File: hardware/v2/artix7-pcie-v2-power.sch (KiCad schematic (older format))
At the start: 40 parts, among them U3 LP5907MFX-1.2, U5 TPS82130SILT, U6 TPS82150SILT, U7 TPS82150SILT, U8 TPS82130SILT, U9 TPS82150SILT

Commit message: v2 hardware : fix isues found by jlcpcb - change 0603 parts to add paste as they are now loaded - fix solder paste/mask issues with TPS power modules
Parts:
- R40, R41: footprint tom-passives:R_0603_1608Metric_NoPaste -> tom-passives:R_0603_1608Metric
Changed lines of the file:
@@
 F 0 "R40" H 1921 6988 40  0000 L CNN
 F 1 "0R" H 1921 6912 40  0000 L CNN
-F 2 "tom-passives:R_0603_1608Metric_NoPaste" H 1921 6874 30  0001 L CNN
+F 2 "tom-passives:R_0603_1608Metric" H 1921 6874 30  0001 L CNN
 F 3 "" H 1850 6950 30  0001 C CNN
 F 4 "C21189" H 1850 6950 50  0001 C CNN "LCSC"
@@
 F 0 "R41" H 2271 6788 40  0000 L CNN
 F 1 "0R" H 2271 6712 40  0000 L CNN
-F 2 "tom-passives:R_0603_1608Metric_NoPaste" H 2271 6674 30  0001 L CNN
+F 2 "tom-passives:R_0603_1608Metric" H 2271 6674 30  0001 L CNN
 F 3 "" H 2200 6750 30  0001 C CNN
 F 4 "C21189" H 2200 6750 50  0001 C CNN "LCSC"

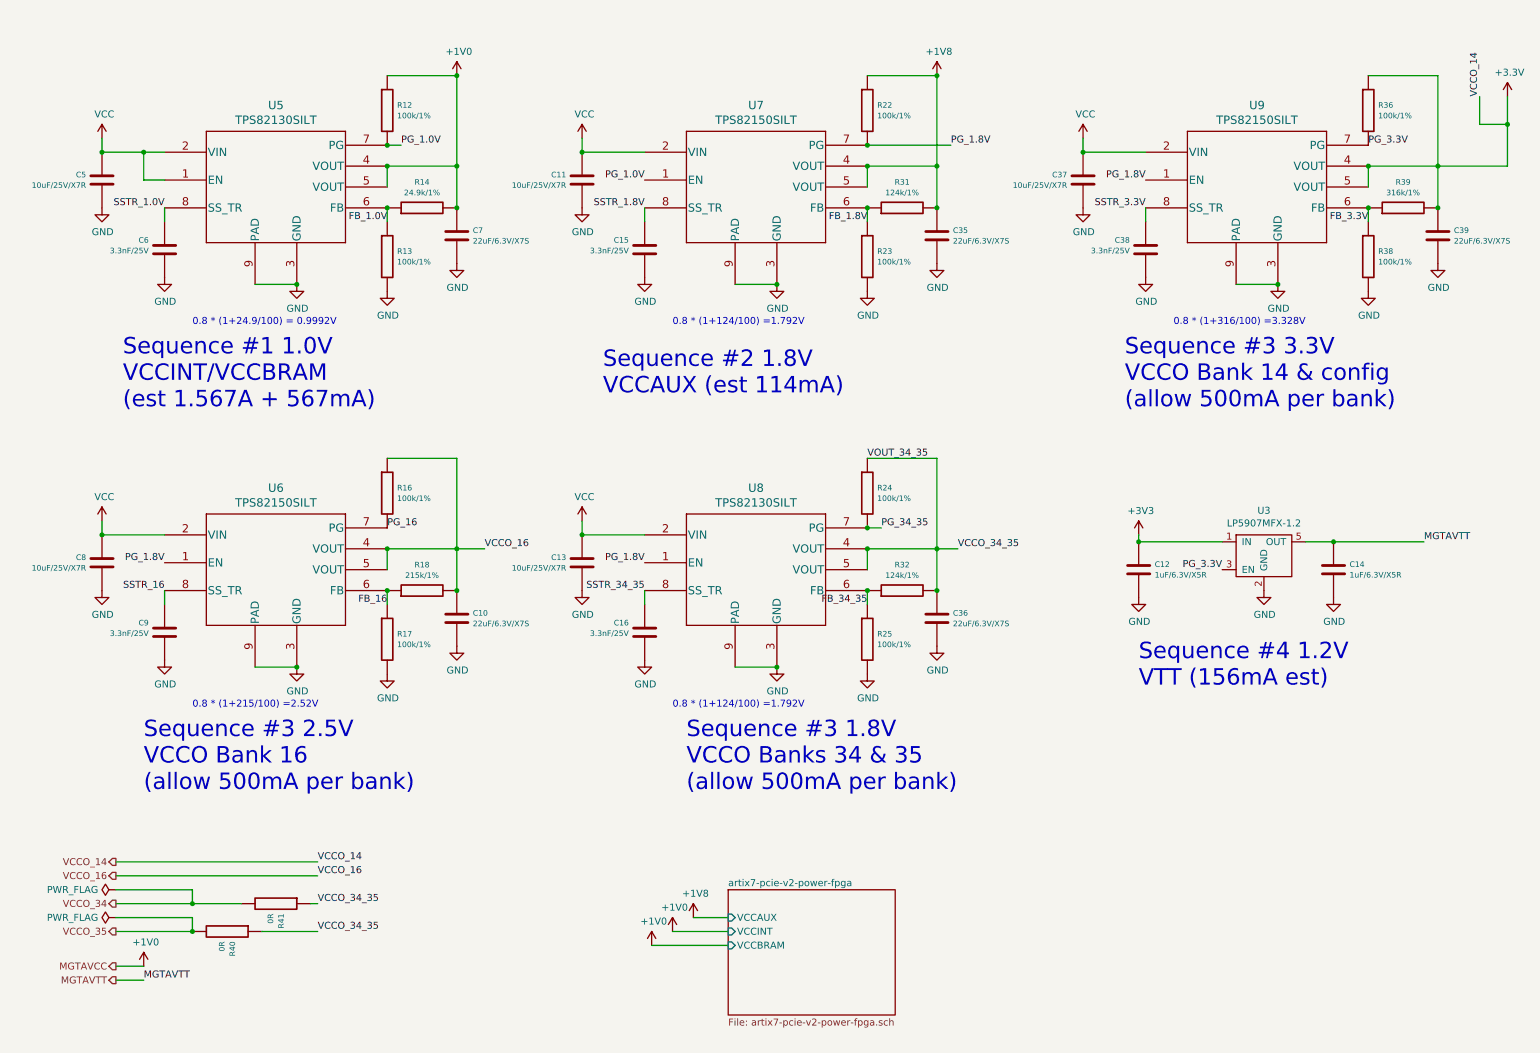
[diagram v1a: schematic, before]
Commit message: JLC power supplies almost routed VCCBRAM to go Need to - check BOM - add power good leds - fix vccbram inc caps - fix 100uF part number - update silk
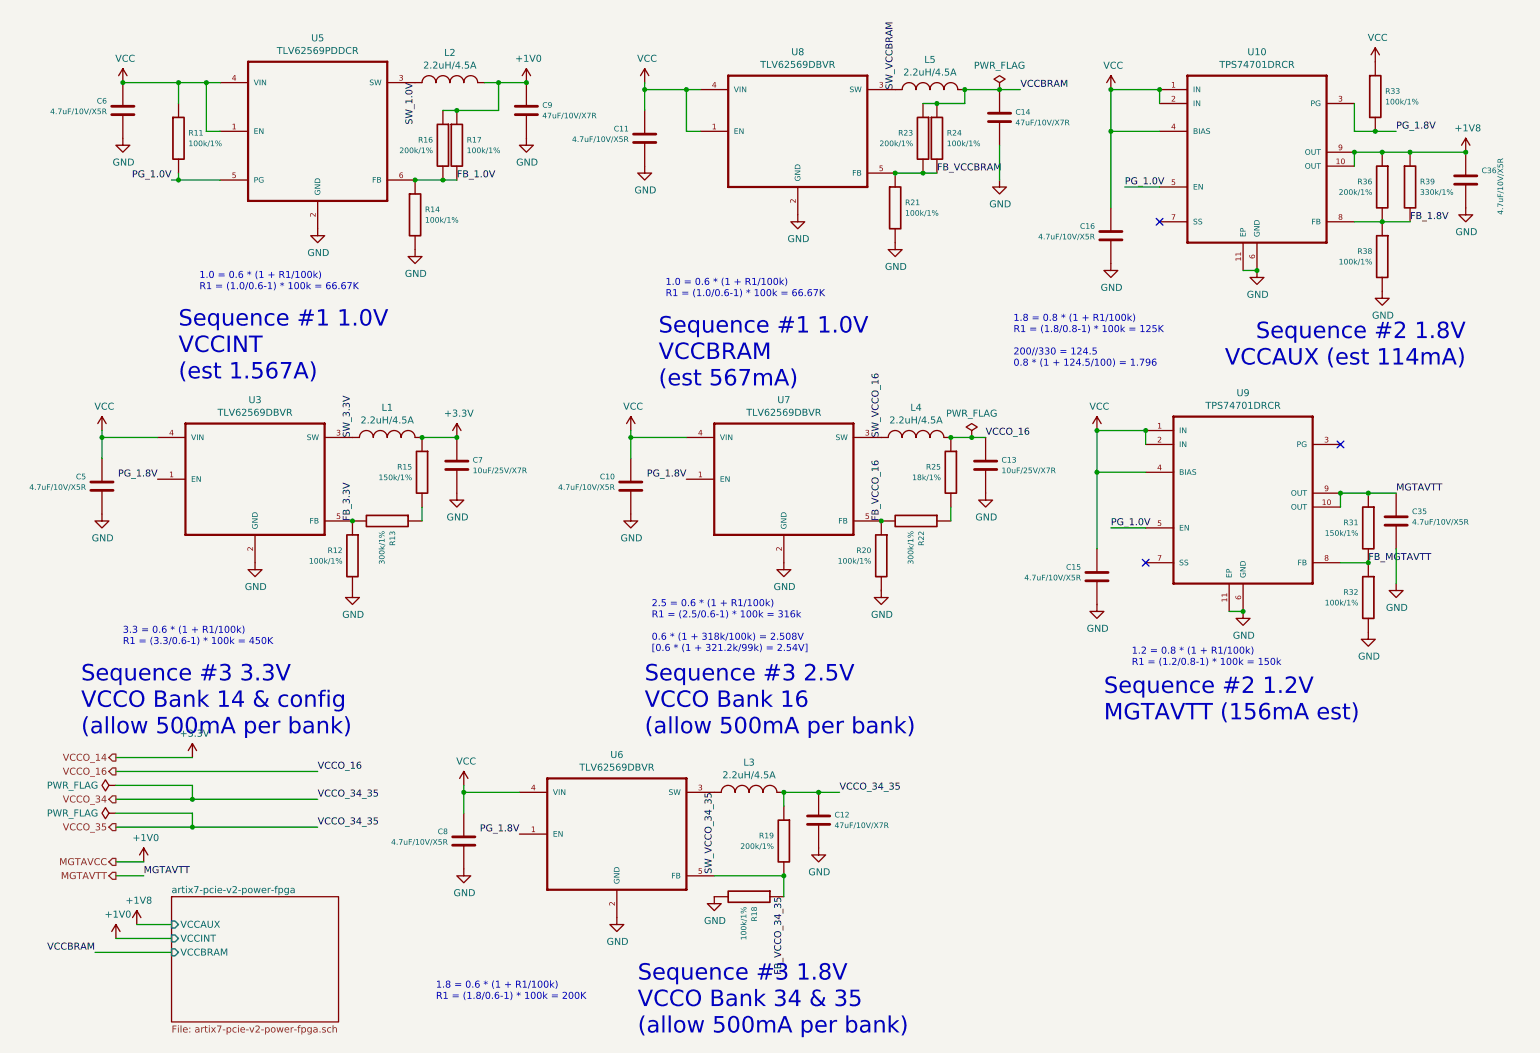
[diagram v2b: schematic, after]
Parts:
- removed C37: 10uF/25V/X7R, tom-passives:C_1206_3216Metric, symbol tom-passives:C
- removed C38: 3.3nF/25V, tom-passives:C_0402_1005Metric, symbol tom-passives:C
- removed C39: 22uF/6.3V/X7S, tom-passives:C_0805_2012Metric, symbol tom-passives:C
- removed R40, R41: 0R, tom-passives:R_0603_1608Metric, symbol tom-passives:R
- removed U3: LP5907MFX-1.2, tom-semiconductors:SOT-23-5, symbol tom-semiconductors:LP5907MFX
- removed U5, U8: TPS82130SILT, tom-modules:TPS82130SILT, symbol tom-modules:TPS821x0SILT
- removed U6, U7, U9: TPS82150SILT, tom-modules:TPS82130SILT, symbol tom-modules:TPS821x0SILT
- added L1, L2, L3, L4, L5: 2.2uH/4.5A, tom-passives:L_MWSA0518S, symbol tom-passives:INDUCTOR_SMALL
- added R11, R20, R21, R33: 100k/1%, tom-passives:R_0402_1005Metric, symbol tom-passives:R
- added R15: 150k/1%, tom-passives:R_0402_1005Metric, symbol tom-passives:R
- added R19: 200k/1%, tom-passives:R_0402_1005Metric, symbol tom-passives:R
- added U10, U9: TPS74701DRCR, artix7-pcie-v2:16624-01YE, symbol artix7-pcie-v2:TPS74701DRCR
- added U3, U6, U7, U8: TLV62569DBVR, artix7-pcie-v2:SOT95P280X145-5N, symbol artix7-pcie-v2:TLV62569DBVR
- added U5: TLV62569PDDCR, artix7-pcie-v2:SOT95P280X110-6N, symbol artix7-pcie-v2:TLV62569PDDCR
- C10, C35, C36: value 22uF/6.3V/X7S -> 4.7uF/10V/X5R; footprint tom-passives:C_0805_2012Metric -> tom-passives:C_0402_1005Metric; LCSC C45783 -> C23733; MFGPN C2012X7S1A226M125AC -> (none); Vendor 1276-1771-1-ND -> 490-5915-1-ND
- C11, C5, C8: value 10uF/25V/X7R -> 4.7uF/10V/X5R; footprint tom-passives:C_1206_3216Metric -> tom-passives:C_0402_1005Metric; LCSC C13585 -> C23733; MFGPN C3216X7R1E106M160AE -> (none); Vendor 399-8153-1-ND -> 490-5915-1-ND
- C12, C14: value 1uF/6.3V/X5R -> 47uF/10V/X7R; footprint tom-passives:C_0402_1005Metric -> tom-passives:C_1206_3216Metric; LCSC C52923 -> C96123
- C15, C16, C6: value 3.3nF/25V -> 4.7uF/10V/X5R; LCSC C26404 -> C23733; Vendor 490-3248-1-ND -> 490-5915-1-ND
- C7: value 22uF/6.3V/X7S -> 10uF/25V/X7R; footprint tom-passives:C_0805_2012Metric -> tom-passives:C_1206_3216Metric; LCSC C45783 -> C13585; MFGPN C2012X7S1A226M125AC -> C3216X7R1E106M160AE; Vendor 1276-1771-1-ND -> 399-8153-1-ND
- C9: value 3.3nF/25V -> 47uF/10V/X7R; footprint tom-passives:C_0402_1005Metric -> tom-passives:C_1206_3216Metric; LCSC C26404 -> C96123; Vendor 490-3248-1-ND -> (none)
- R13, R22: value 100k/1% -> 300k/1%; LCSC C25741 -> C25774
- R14: value 24.9k/1% -> 100k/1%; LCSC C25874 -> C25741; Vendor RMCF0402FT24K9CT-ND -> (none)
- R16, R23, R36: value 100k/1% -> 200k/1%; LCSC C25741 -> C25764
- R18: value 215k/1% -> 100k/1%; LCSC C11489 -> C25741; Vendor RMCF0402FT215KCT-ND -> (none)
- R25: value 100k/1% -> 18k/1%; LCSC C25741 -> C25762
- R31: value 124k/1% -> 150k/1%; LCSC C36777 -> C25755; Vendor 2019-RK73H1ETTP1243FCT-ND -> (none)
- R32: value 124k/1% -> 100k/1%; LCSC C36777 -> C25741; Vendor 2019-RK73H1ETTP1243FCT-ND -> (none)
- R39: value 316k/1% -> 330k/1%; LCSC C25777 -> C25778; Vendor 738-RMCF0402FT316KCT-ND -> (none)
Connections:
- net PG_16 is gone; now on net FB_1.0V: R16.2
- net PG_3.3V is gone; now on net FB_1.8V: R36.2
- net SSTR_1.0V is gone; now on net VCC: C6.2
- net SSTR_1.8V is gone; now on net VCC: C15.2
- net SSTR_16 is gone; now on net +1V0: C9.2
- net SSTR_34_35 is gone; now on net VCC: C16.2
- net +1V0: now also R16.1, R17.1, L2.2; no longer C7.1, R12.1, R14.2
- net +1V8: now also C36.2, R36.1, R39.1, U10.10 (OUT), U10.9 (OUT); no longer C35.1, R22.1, R31.2
- net +3V3: now also C7.2, L1.2, R15.1; no longer C12.1, R36.1, R39.2
- net FB_1.0V: now also R17.2, U5.6 (FB); no longer R13.1
- net FB_1.8V: now also R38.1, R39.2, U10.8 (FB); no longer R23.1, R31.1
- net FB_3.3V: now also R12.1, R13.2, U3.5 (FB); no longer R38.1, R39.1
- net GND: now also C10.1, C12.1, C14.1, C35.1, C36.1, C7.1, R12.2, R14.2, R18.2, R32.2, R20.2, R21.2, U10.11 (EP), U10.6 (GND), U3.2 (GND), U5.2 (GND), U6.2 (GND), U7.2 (GND), U8.2 (GND), U9.11 (EP), U9.6 (GND); no longer C10.2, C12.2, C14.2, C35.2, C36.2, C7.2, R13.2, R17.2, R23.2, R25.2
- net MGTAVTT: now also C35.2, R31.1, U9.10 (OUT), U9.9 (OUT); no longer C14.1
- net PG_1.0V: now also R11.2, U10.5 (EN), U5.5 (PG), U9.5 (EN); no longer R12.2
- net PG_1.8V: now also R33.2, U10.3 (PG), U3.1 (EN), U6.1 (EN), U7.1 (EN); no longer R22.2
- net VCC: now also C10.2, R11.1, R33.1, U10.1 (IN), U10.2 (IN), U10.4 (BIAS), U3.4 (VIN), U5.1 (EN), U5.4 (VIN), U6.4 (VIN), U7.4 (VIN), U8.1 (EN), U8.4 (VIN), U9.1 (IN), U9.2 (IN), U9.4 (BIAS); no longer C13.2
- net VCCO_16: now also C13.2, R25.1, L4.2; no longer C10.1, R16.1, R18.2
- net VCCO_34: now also C12.2, L3.2, R19.1
- net FB_16 renamed FB_VCCO_34_35
- net FB_VCCO_34_35: now also R19.2, U6.5 (FB); no longer R17.1
- net FB_34_35 renamed FB_MGTAVTT
- net FB_MGTAVTT: now also R31.2, U9.8 (FB); no longer R25.1
- net PG_34_35 renamed FB_VCCBRAM
- net FB_VCCBRAM: now also R23.2, R21.1, U8.5 (FB)
- removed net VCCO_34_35: C36.1, R24.1, R32.2
- new net: R13.1, R15.2
- new net: R22.1, R25.2
- new net FB_VCCO_16: R20.1, R22.2, U7.5 (FB)
- new net SW_1.0V: L2.1, U5.3 (SW)
- new net SW_3.3V: L1.1, U3.3 (SW)
- new net SW_VCCBRAM: L5.1, U8.3 (SW)
- new net SW_VCCO_16: L4.1, U7.3 (SW)
- new net SW_VCCO_34_35: L3.1, U6.3 (SW)
- new net VCCBRAM: C14.2, L5.2, R23.1, R24.1
- no-connect marks 0 -> 3
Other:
- note added: "1.0 = 0.6 * (1 + R1/100k)\nR1 = (1.0/0.6-1) * 100k = 66.67K"
- note added: "1.2 = 0.8 * (1 + R1/100k)\nR1 = (1.2/0.8-1) * 100k = 150k"
- note added: "1.8 = 0.6 * (1 + R1/100k)\nR1 = (1.8/0.6-1) * 100k = 200K"
- note added: "1.8 = 0.8 * (1 + R1/100k)\nR1 = (1.8/0.8-1) * 100k = 125K\n\n200//330 = 124.5\n0.8 * (1 + 124.5/100) = 1.796"
- note added: "2.5 = 0.6 * (1 + R1/100k)\nR1 = (2.5/0.6-1) * 100k = 316k\n\n0.6 * (1 + 318k/100k) = 2.508V\n[0.6 * (1 + 321.2k/99k) = 2.54V]"
- note added: "3.3 = 0.6 * (1 + R1/100k)\nR1 = (3.3/0.6-1) * 100k = 450K"
- note added: "Sequence #1 1.0V\nVCCBRAM\n(est 567mA)"
- note added: "Sequence #1 1.0V\nVCCINT\n(est 1.567A)"
- note added: "Sequence #2 1.2V\nMGTAVTT (156mA est)"
- note added: "Sequence #3 1.8V\nVCCO Bank 34 & 35\n(allow 500mA per bank)"
- note removed: "0.8 * (1+124/100) =1.792V"
- note removed: "0.8 * (1+215/100) =2.52V"
- note removed: "0.8 * (1+24.9/100) = 0.9992V"
- note removed: "0.8 * (1+316/100) =3.328V"
- note removed: "Sequence #1 1.0V\nVCCINT/VCCBRAM\n(est 1.567A + 567mA)"
- note removed: "Sequence #3 1.8V\nVCCO Banks 34 & 35\n(allow 500mA per bank)"
- note removed: "Sequence #4 1.2V\nVTT (156mA est)"

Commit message: v2 hardware updates: fixed inductor footprint, updates for DFA
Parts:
- L1, L2, L3, L4, L5: LCSC C169184 -> C408345; MPN MWSA0402-2R2MT -> MWSA0518S-2R2MT
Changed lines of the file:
@@
 F 2 "tom-passives:L_MWSA0518S" H 3450 981 60  0001 C CNN
 F 3 "" H 3450 850 60  0001 C CNN
-F 4 "C169184" H 3450 850 50  0001 C CNN "LCSC"
-F 5 "MWSA0402-2R2MT" H 3450 850 50  0001 C CNN "MPN"
+F 4 "C408345" H 3450 850 50  0001 C CNN "LCSC"
+F 5 "MWSA0518S-2R2MT" H 3450 850 50  0001 C CNN "MPN"
 	1    3450 850
 	1    0    0    -1
@@
 F 2 "tom-passives:L_MWSA0518S" H 3000 3531 60  0001 C CNN
 F 3 "" H 3000 3400 60  0001 C CNN
-F 4 "C169184" H 3000 3400 50  0001 C CNN "LCSC"
-F 5 "MWSA0402-2R2MT" H 3000 3400 50  0001 C CNN "MPN"
+F 4 "C408345" H 3000 3400 50  0001 C CNN "LCSC"
+F 5 "MWSA0518S-2R2MT" H 3000 3400 50  0001 C CNN "MPN"
 	1    3000 3400
 	1    0    0    -1
@@
 F 2 "tom-passives:L_MWSA0518S" H 6900 1031 60  0001 C CNN
 F 3 "" H 6900 900 60  0001 C CNN
-F 4 "C169184" H 6900 900 50  0001 C CNN "LCSC"
-F 5 "MWSA0402-2R2MT" H 6900 900 50  0001 C CNN "MPN"
+F 4 "C408345" H 6900 900 50  0001 C CNN "LCSC"
+F 5 "MWSA0518S-2R2MT" H 6900 900 50  0001 C CNN "MPN"
 	1    6900 900
 	1    0    0    -1
@@
 F 2 "tom-passives:L_MWSA0518S" H 6800 3531 60  0001 C CNN
 F 3 "" H 6800 3400 60  0001 C CNN
-F 4 "C169184" H 6800 3400 50  0001 C CNN "LCSC"
-F 5 "MWSA0402-2R2MT" H 6800 3400 50  0001 C CNN "MPN"
+F 4 "C408345" H 6800 3400 50  0001 C CNN "LCSC"
+F 5 "MWSA0518S-2R2MT" H 6800 3400 50  0001 C CNN "MPN"
 	1    6800 3400
 	1    0    0    -1
@@
 F 2 "tom-passives:L_MWSA0518S" H 5600 6081 60  0001 C CNN
 F 3 "" H 5600 5950 60  0001 C CNN
-F 4 "C169184" H 5600 5950 50  0001 C CNN "LCSC"
-F 5 "MWSA0402-2R2MT" H 5600 5950 50  0001 C CNN "MPN"
+F 4 "C408345" H 5600 5950 50  0001 C CNN "LCSC"
+F 5 "MWSA0518S-2R2MT" H 5600 5950 50  0001 C CNN "MPN"
 	1    5600 5950
 	1    0    0    -1
